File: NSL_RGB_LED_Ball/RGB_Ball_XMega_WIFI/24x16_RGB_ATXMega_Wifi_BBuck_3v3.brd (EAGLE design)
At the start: 46.4 x 123.7 mm, 118 parts, among them IC2 TLC5947XLP, IC3 TLC5947XLP, IC4 TLC5947XLP, IC5 MCP73123, IC6 CC3000, IC7 MMA7455L, IC8 OPA344, IC9 TPS6300X, X1 NX3225GA-16.000M-STD-CRG-2

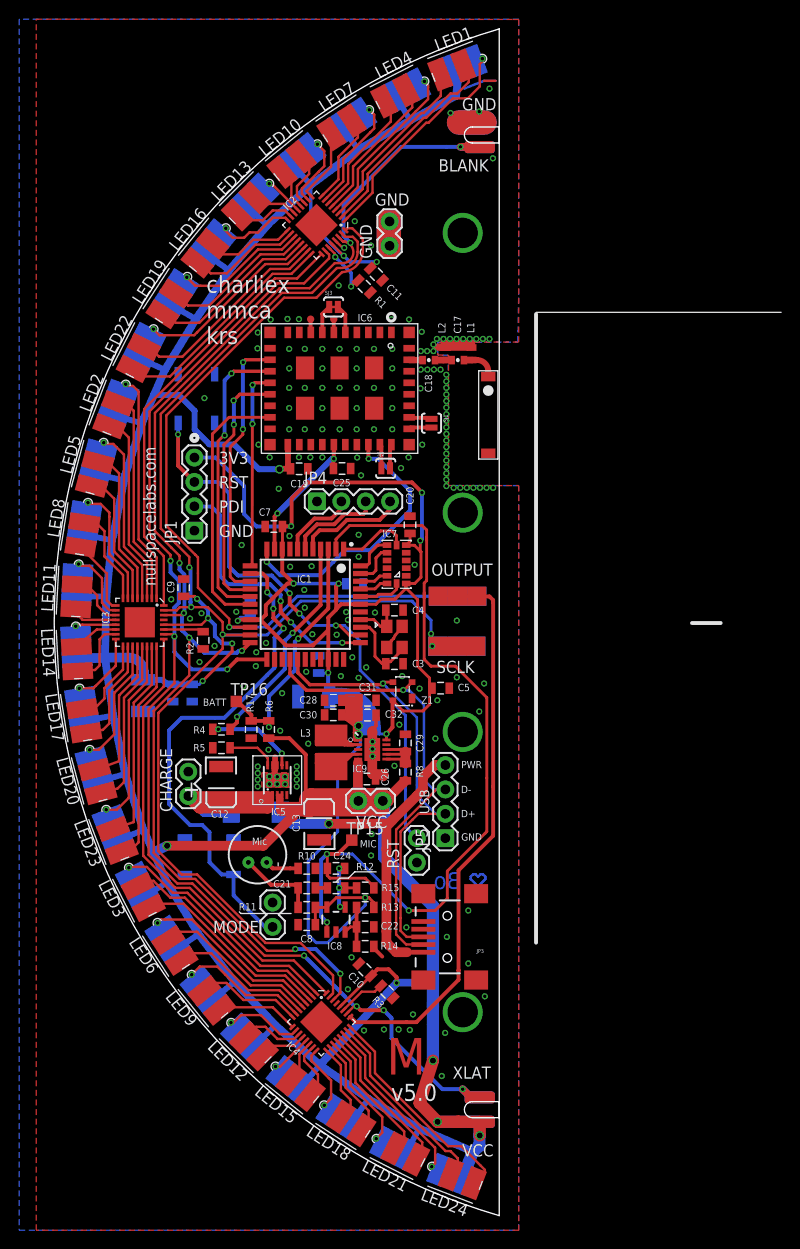
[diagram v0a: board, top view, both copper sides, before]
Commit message: 
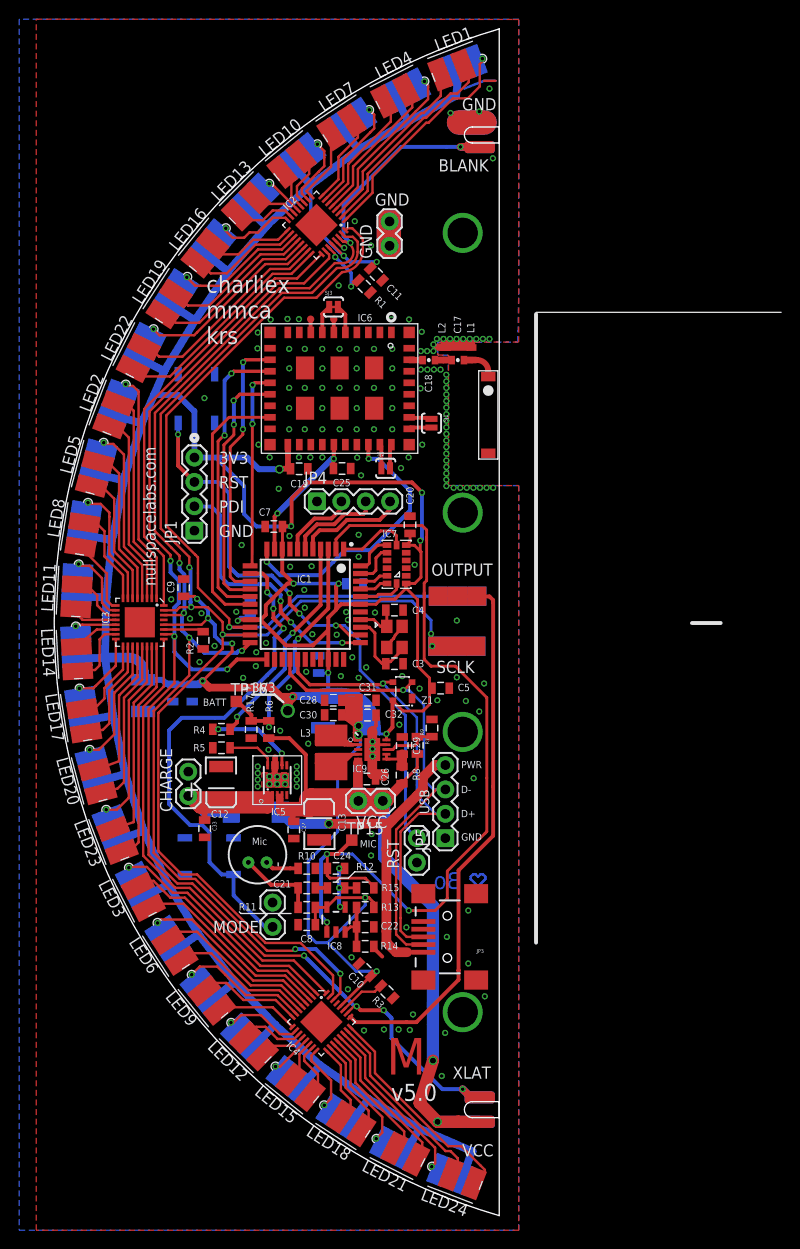
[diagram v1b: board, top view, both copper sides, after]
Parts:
- added C27, C33: 10uF, 24x16_RGB:0805
- added R7: 100K, CH_passive:0805
- added R9: 340K, CH_passive:0805
- moved C23 1.87 mm to (-36.1, -9.35), turned to 90 degrees
- moved R8 0.47 mm to (-27.9, -15.9)
- moved C29 0.43 mm to (-27.9, -12.9)
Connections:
- new net VINA: IC9.8, R7.1, R9.1
- net +3V3: now also C10.1, C11.1, C14.A, C15.1, C16.1, C19.2, C9.1, IC2.28, IC3.28, IC4.28, IC6.P$19, LED1.A, LED10.A, LED11.A, LED12.A, LED13.A, LED14.A, LED15.A, LED16.A, LED17.A, LED18.A, LED19.A, LED2.A, LED20.A, LED21.A, LED22.A, LED23.A, LED24.A, LED3.A, LED4.A, LED5.A, LED6.A, LED7.A, LED8.A, LED9.A
- net CHARGE: now also C33.1
- net GND: now also C27.2, C33.2, R9.2
- net N$32: no longer IC9.8
- net VCC: now also C27.1, R7.2; no longer C10.1, C11.1, C14.A, C15.1, C16.1, C19.2, C9.1, IC2.28, IC3.28, IC4.28, IC6.P$19, LED1.A, LED10.A, LED11.A, LED12.A, LED13.A, LED14.A, LED15.A, LED16.A, LED17.A, LED18.A, LED19.A, LED2.A, LED20.A, LED21.A, LED22.A, LED23.A, LED24.A, LED3.A, LED4.A, LED5.A, LED6.A, LED7.A, LED8.A, LED9.A
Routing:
- net VCC: track 454.6 -> 128.8 mm, vias 12 -> 2
- net +3V3: track 223.1 -> 539.8 mm, vias 11 -> 21
- net VINA: track 0.00 -> 5.73 mm
- net N$32: track 7.58 -> 4.13 mm
- net CHARGE: track 34.2 -> 37.5 mm
- net GND: track 37.8 -> 39.7 mm
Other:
- board text added: "+3V3"

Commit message: 
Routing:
- net +3V3: track 539.8 -> 540.4 mm
- net GND: vias 177 -> 180
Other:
- board text added: "v5.1"
- board text removed: "v5.0"

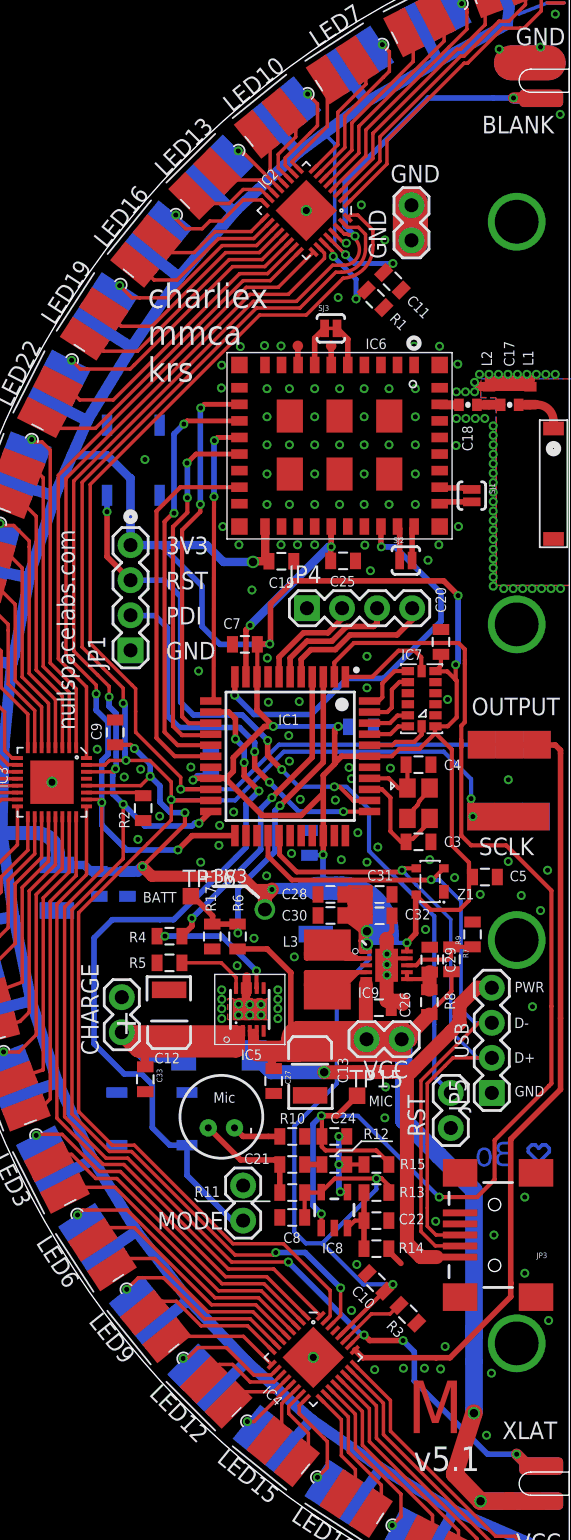
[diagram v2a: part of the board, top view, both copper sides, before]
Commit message: 
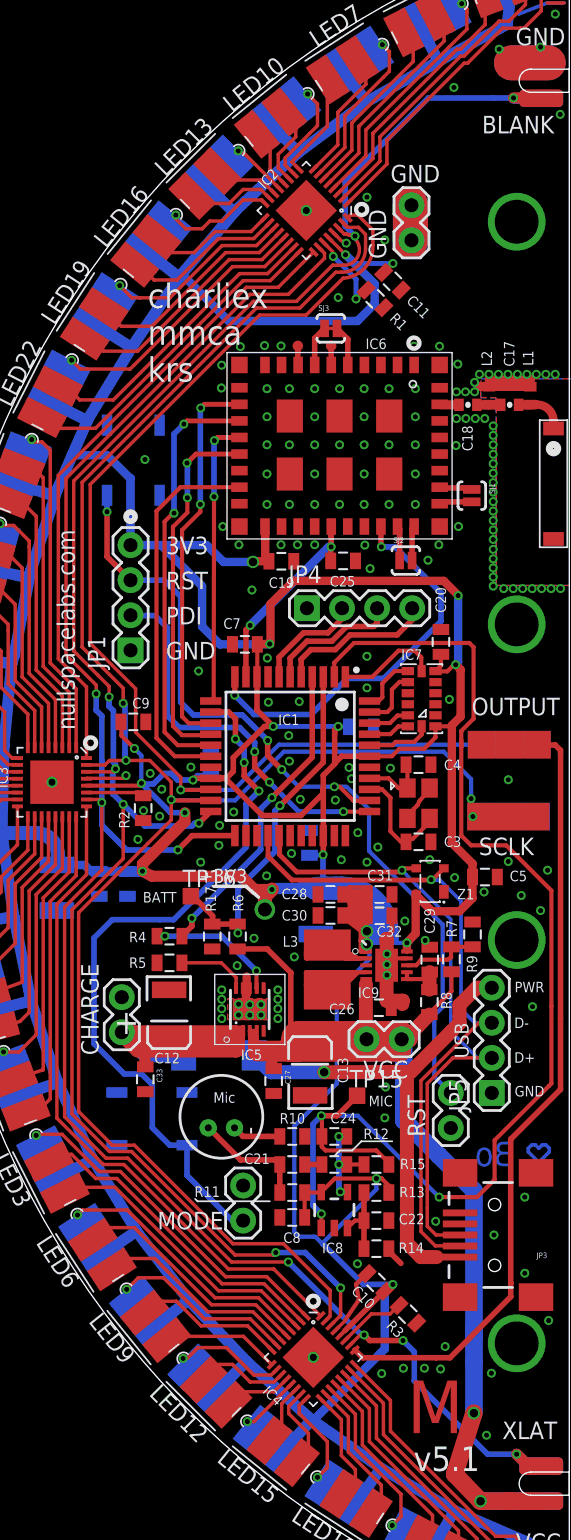
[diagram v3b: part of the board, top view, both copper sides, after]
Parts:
- moved C9 1.52 mm to (-49.4, 4.37), turned to 0 degrees
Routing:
- net +3V3: track 540.4 -> 577.0 mm
- net GND: track 39.7 -> 47.8 mm, vias 180 -> 182
- net MIC: track 91.3 -> 92.3 mm
- net RST: track 62.1 -> 62.6 mm

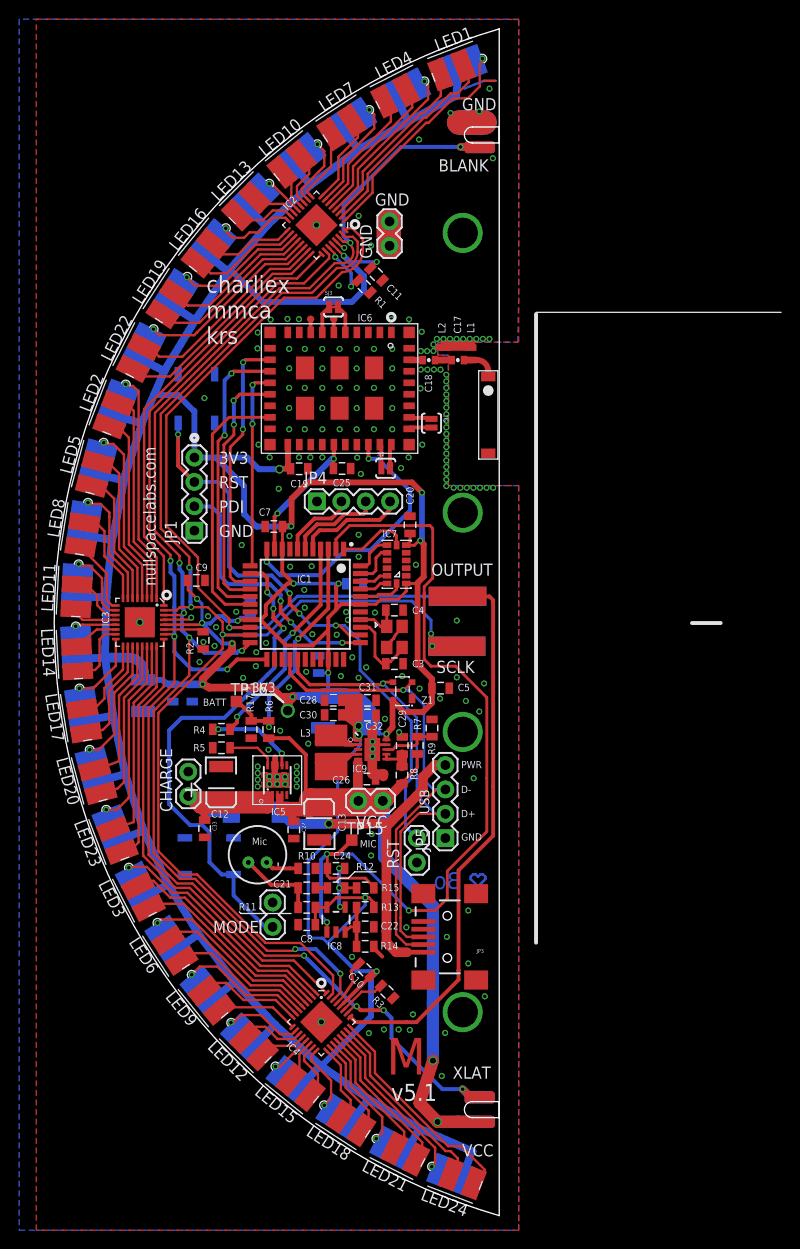
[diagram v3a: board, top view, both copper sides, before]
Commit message: 
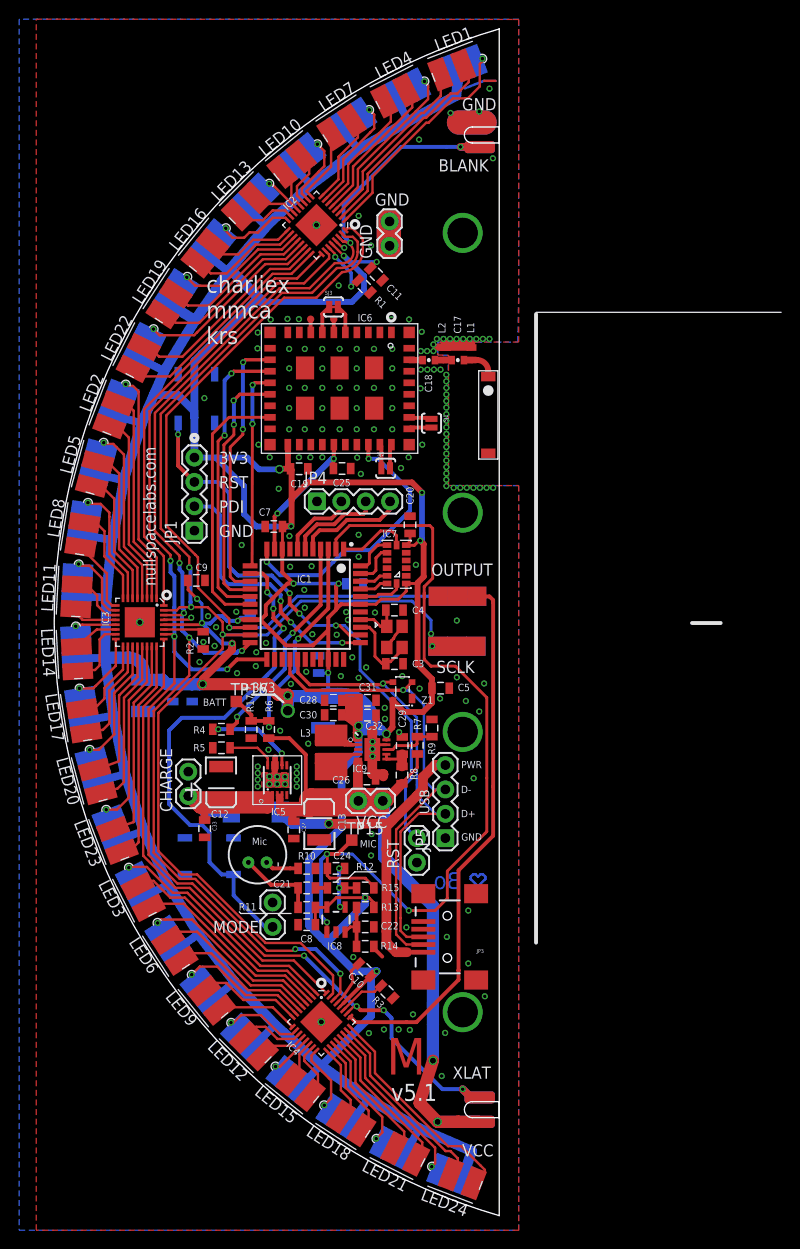
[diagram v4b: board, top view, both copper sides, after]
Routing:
- net +3V3: track 577.0 -> 598.7 mm
- net GND: vias 182 -> 183
